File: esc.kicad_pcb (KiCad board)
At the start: 4 copper layers, 68.3 x 63.8 mm, 73 parts, among them J1 Conn_01x02, J2 Screw_Terminal_01x01, J3 Screw_Terminal_01x01, J4 Screw_Terminal_01x01, J5 3220-10-0100-00, Q1 SIR182DP-T1-RE3, Q2 SIR182DP-T1-RE3, Q3 SIR182DP-T1-RE3, Q4 SIR182DP-T1-RE3, Q5 SIR182DP-T1-RE3, Q6 SIR182DP-T1-RE3, SW1 RotaryEncoder, U1 TPS7A20xxxDQN, U2 STM32G484CETx, U3 TPS562201DDCR, U4 TVS0500DRV, U5 IR2103STRPBF, U6 IR2103STRPBF, U7 IR2103STRPBF, Y1 32.768KHz

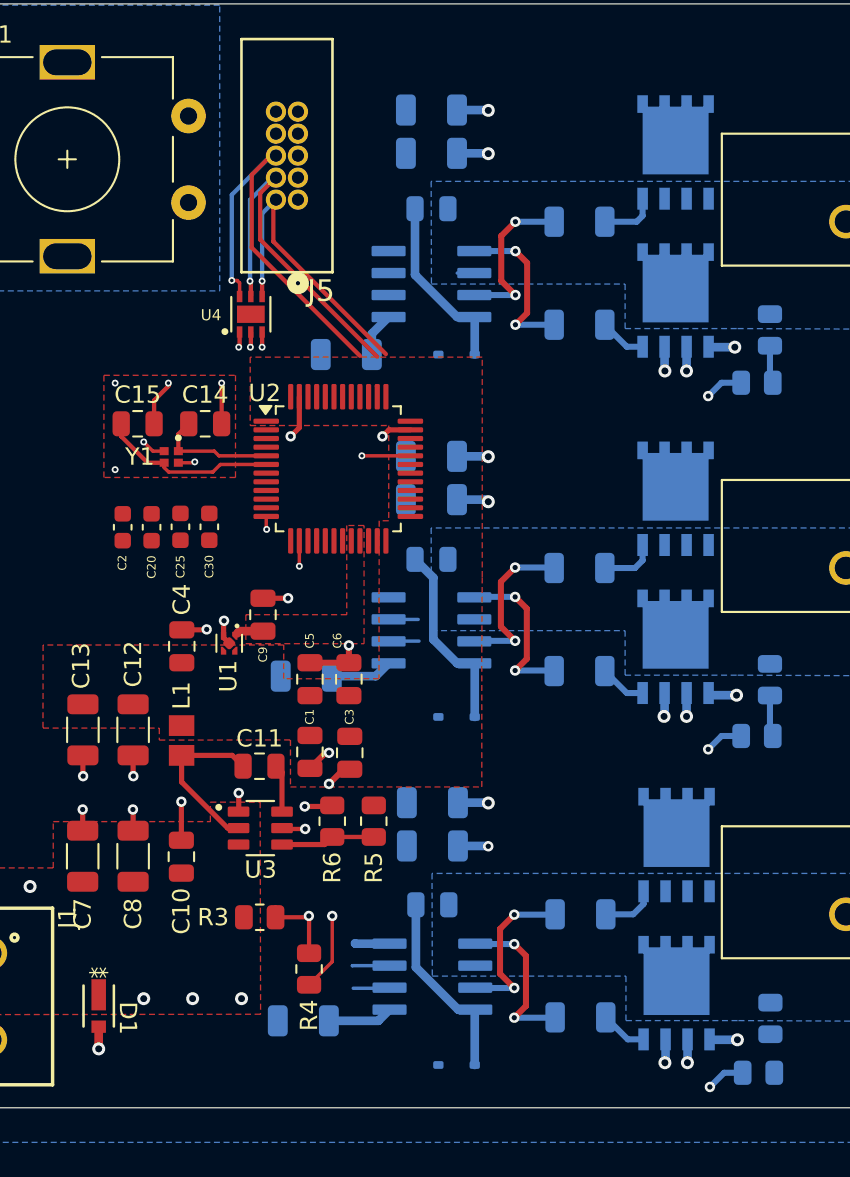
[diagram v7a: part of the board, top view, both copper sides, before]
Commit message: routing cleanup
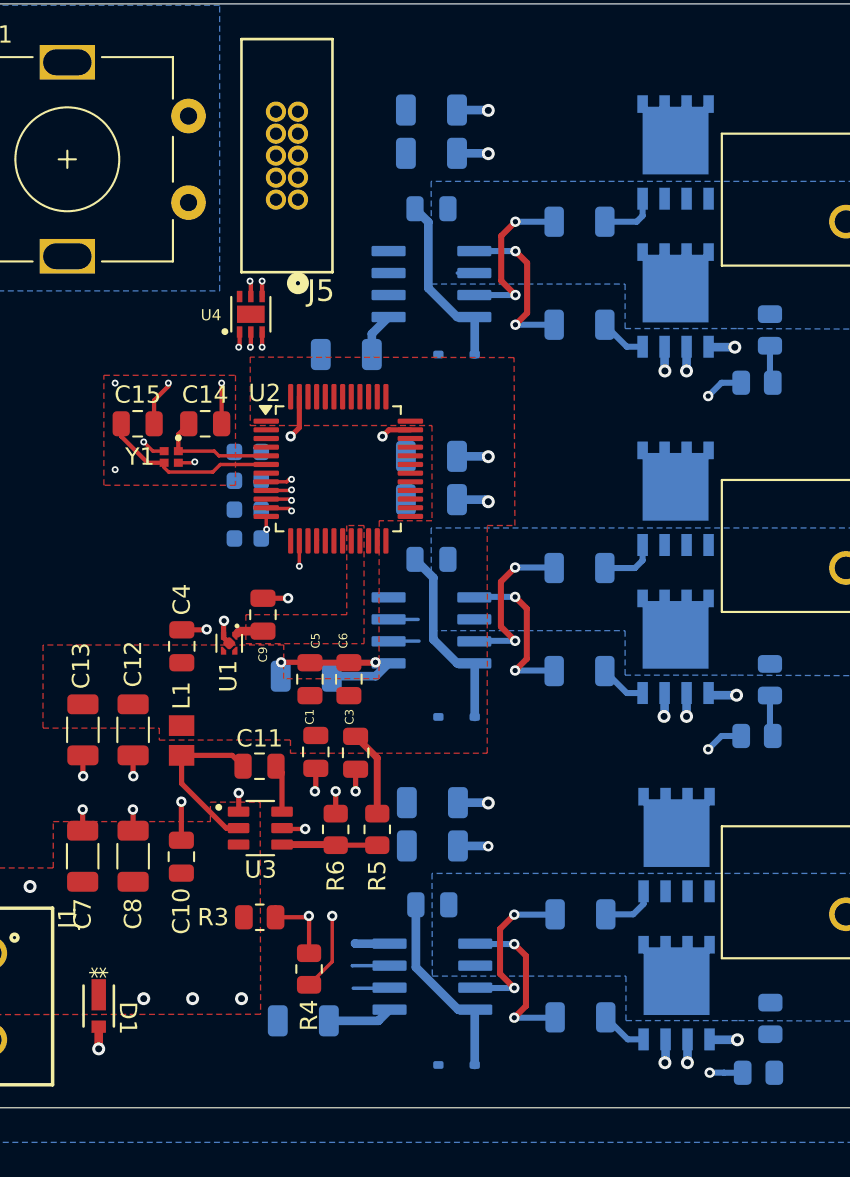
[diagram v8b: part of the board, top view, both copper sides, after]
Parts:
- C2, C20, C25, C30: moved to B.Cu
- moved C2 8.43 mm to (131.6, 88.3), turned to 180 degrees
- moved C20 6.17 mm to (131.6, 90.0), turned to 180 degrees
- moved C25 4.02 mm to (131.6, 91.6), turned to 180 degrees
- moved C30 2.33 mm to (131.6, 93.3), turned to 180 degrees
- moved R5 0.52 mm to (139.1, 110.1)
- moved R6 0.52 mm to (136.7, 110.1)
- moved C5 0.34 mm to (135.6, 105.6)
- moved C6 0.34 mm to (137.8, 105.7)
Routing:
- net /STM32/W_HIN: track 37.2 -> 2.13 mm, vias 1 -> 0
- net /STM32/SWO: track 24.6 -> 0.00 mm, vias 1 -> 0
- net /STM32/SWCLK: track 22.4 -> 1.52 mm
- net /STM32/SWDIO: track 17.6 -> 0.92 mm
- net /STM32/ENC_A: track 38.4 -> 45.8 mm
- net /STM32/ENC_B: track 37.3 -> 42.9 mm
- net +3V3: track 0.00 -> 4.98 mm
- net /STM32/W_VSENSE: track 0.00 -> 1.52 mm, vias 0 -> 1
- net /PWR/VCC_SENSE: track 1.98 -> 3.50 mm, vias 0 -> 1
- net /STM32/U_VSENSE: track 2.20 -> 3.69 mm, vias 0 -> 1
- net /STM32/V_VSENSE: track 2.40 -> 3.88 mm, vias 0 -> 1
- net GND: track 74.6 -> 75.8 mm, vias 45 -> 46
